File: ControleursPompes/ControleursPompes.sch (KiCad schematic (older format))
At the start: 54 parts, among them J1 SWD, J2 PWR_IN, J3 I2C 5V, J4 I2C 3.3V, J5 ARIG Interf, Q1 BSS138, Q2 BSS138, SW1 Reset, SW2 Reset, SW3 Reset, U1 AMS1117-3.3, U2 STM32F103C8Tx, Y1 16Mhz

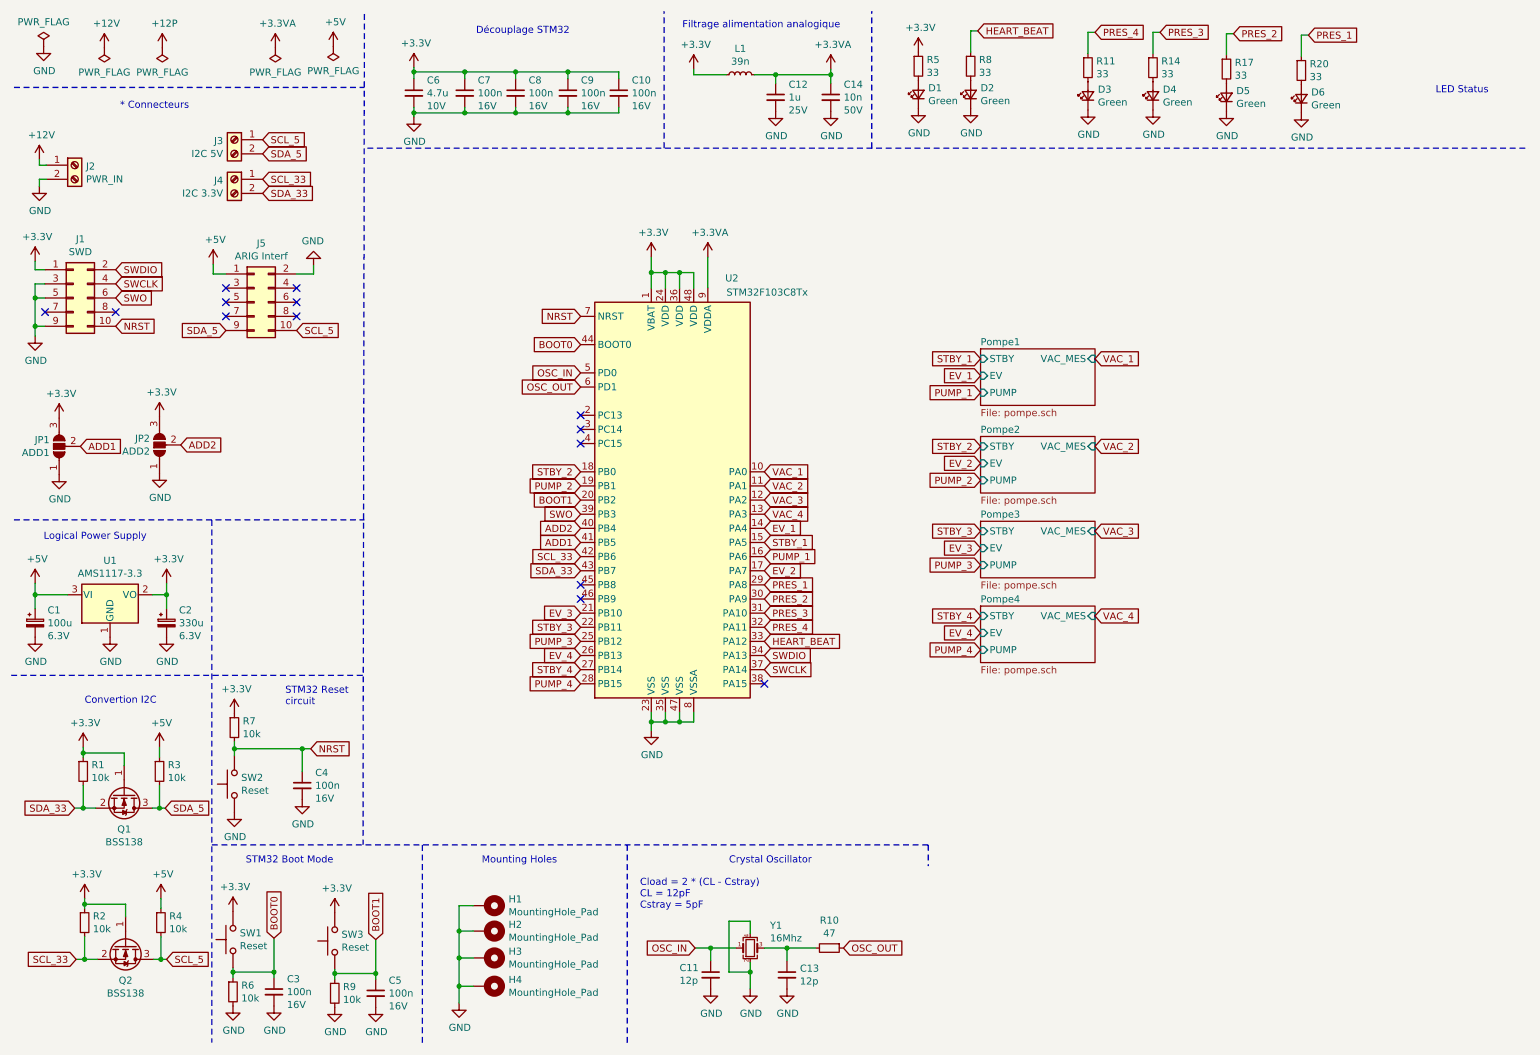
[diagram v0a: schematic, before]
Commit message: Ajout bornier alim 5V sur controleur pompes
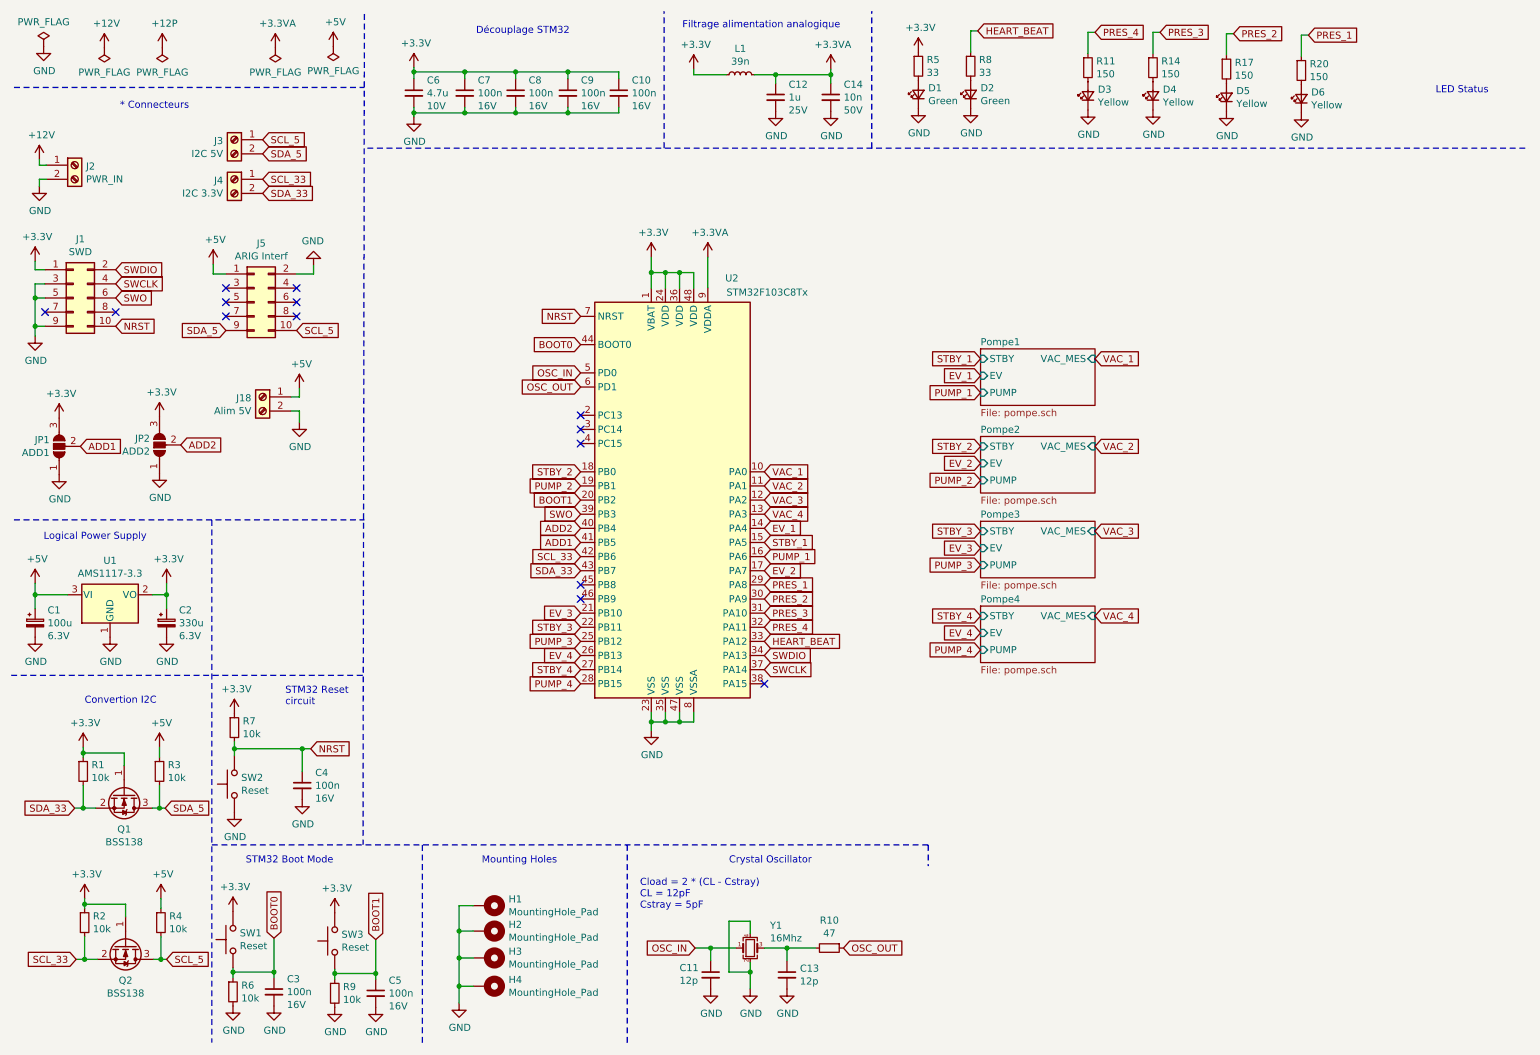
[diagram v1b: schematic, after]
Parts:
- added J18: Alim 5V, TerminalBlock_Phoenix:TerminalBlock_Phoenix_MPT-0,5-2-2.54_1x02_P2.54mm_Horizontal, symbol Connector:Screw_Terminal_01x02
- D3, D4, D5, D6: value Green -> Yellow; LCSC Part C63855 -> C74346
- R11, R14, R17, R20: value 33 -> 150; LCSC Part C17634 -> C17471
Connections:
- net +5V: now also J18.1 (Pin_1)
- net GND: now also J18.2 (Pin_2)
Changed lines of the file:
@@
 P 8100 880
 F 0 "R11" H 8159 926 50  0000 L CNN
-F 1 "33" H 8159 835 50  0000 L CNN
+F 1 "150" H 8159 835 50  0000 L CNN
 F 2 "Resistor_SMD:R_0805_2012Metric_Pad1.20x1.40mm_HandSolder" H 8100 880 50  0001 C CNN
 F 3 "~" H 8100 880 50  0001 C CNN
-F 4 "C17634" H 8100 880 50  0001 C CNN "LCSC Part"
+F 4 "C17471" H 8100 880 50  0001 C CNN "LCSC Part"
 	1    8100 880
 	1    0    0    -1
@@
 P 8100 1080
 F 0 "D3" V 8146 1010 50  0000 R CNN
-F 1 "Green" V 8055 1010 50  0000 R CNN
+F 1 "Yellow" V 8055 1010 50  0000 R CNN
 F 2 "LED_SMD:LED_0805_2012Metric_Pad1.15x1.40mm_HandSolder" V 8100 1080 50  0001 C CNN
 F 3 "~" V 8100 1080 50  0001 C CNN
-F 4 "C63855" H 8100 1080 50  0001 C CNN "LCSC Part"
+F 4 "C74346" H 8100 1080 50  0001 C CNN "LCSC Part"
 	1    8100 1080
 	0    -1   -1   0
@@
 P 8560 880
 F 0 "R14" H 8619 926 50  0000 L CNN
-F 1 "33" H 8619 835 50  0000 L CNN
+F 1 "150" H 8619 835 50  0000 L CNN
 F 2 "Resistor_SMD:R_0805_2012Metric_Pad1.20x1.40mm_HandSolder" H 8560 880 50  0001 C CNN
 F 3 "~" H 8560 880 50  0001 C CNN
-F 4 "C17634" H 8560 880 50  0001 C CNN "LCSC Part"
+F 4 "C17471" H 8560 880 50  0001 C CNN "LCSC Part"
 	1    8560 880
 	1    0    0    -1
@@
 P 8560 1080
 F 0 "D4" V 8606 1010 50  0000 R CNN
-F 1 "Green" V 8515 1010 50  0000 R CNN
+F 1 "Yellow" V 8515 1010 50  0000 R CNN
 F 2 "LED_SMD:LED_0805_2012Metric_Pad1.15x1.40mm_HandSolder" V 8560 1080 50  0001 C CNN
 F 3 "~" V 8560 1080 50  0001 C CNN
-F 4 "C63855" H 8560 1080 50  0001 C CNN "LCSC Part"
+F 4 "C74346" H 8560 1080 50  0001 C CNN "LCSC Part"
 	1    8560 1080
 	0    -1   -1   0
@@
 P 9080 890
 F 0 "R17" H 9139 936 50  0000 L CNN
-F 1 "33" H 9139 845 50  0000 L CNN
+F 1 "150" H 9139 845 50  0000 L CNN
 F 2 "Resistor_SMD:R_0805_2012Metric_Pad1.20x1.40mm_HandSolder" H 9080 890 50  0001 C CNN
 F 3 "~" H 9080 890 50  0001 C CNN
-F 4 "C17634" H 9080 890 50  0001 C CNN "LCSC Part"
+F 4 "C17471" H 9080 890 50  0001 C CNN "LCSC Part"
 	1    9080 890
 	1    0    0    -1
@@
 P 9080 1090
 F 0 "D5" V 9126 1020 50  0000 R CNN
-F 1 "Green" V 9035 1020 50  0000 R CNN
+F 1 "Yellow" V 9035 1020 50  0000 R CNN
 F 2 "LED_SMD:LED_0805_2012Metric_Pad1.15x1.40mm_HandSolder" V 9080 1090 50  0001 C CNN
 F 3 "~" V 9080 1090 50  0001 C CNN
-F 4 "C63855" H 9080 1090 50  0001 C CNN "LCSC Part"
+F 4 "C74346" H 9080 1090 50  0001 C CNN "LCSC Part"
 	1    9080 1090
 	0    -1   -1   0
@@
 P 9610 900
 F 0 "R20" H 9669 946 50  0000 L CNN
-F 1 "33" H 9669 855 50  0000 L CNN
+F 1 "150" H 9669 855 50  0000 L CNN
 F 2 "Resistor_SMD:R_0805_2012Metric_Pad1.20x1.40mm_HandSolder" H 9610 900 50  0001 C CNN
 F 3 "~" H 9610 900 50  0001 C CNN
-F 4 "C17634" H 9610 900 50  0001 C CNN "LCSC Part"
+F 4 "C17471" H 9610 900 50  0001 C CNN "LCSC Part"
 	1    9610 900
 	1    0    0    -1
@@
 P 9610 1100
 F 0 "D6" V 9656 1030 50  0000 R CNN
-F 1 "Green" V 9565 1030 50  0000 R CNN
+F 1 "Yellow" V 9565 1030 50  0000 R CNN
 F 2 "LED_SMD:LED_0805_2012Metric_Pad1.15x1.40mm_HandSolder" V 9610 1100 50  0001 C CNN
 F 3 "~" V 9610 1100 50  0001 C CNN
-F 4 "C63855" H 9610 1100 50  0001 C CNN "LCSC Part"
+F 4 "C74346" H 9610 1100 50  0001 C CNN "LCSC Part"
 	1    9610 1100
 	0    -1   -1   0
@@
 Wire Notes Line
 	3000 1450 11220 1450
+$Comp
+L Connector:Screw_Terminal_01x02 J18
+U 1 1 60671C10
+P 2260 3210
+F 0 "J18" H 2340 3202 50  0000 L CNN
+F 1 "Alim 5V" H 2340 3111 50  0000 L CNN
+F 2 "TerminalBlock_Phoenix:TerminalBlock_Phoenix_MPT-0,5-2-2.54_1x02_P2.54mm_Horizontal" H 2260 3210 50  0001 C CNN
+F 3 "~" H 2260 3210 50  0001 C CNN
+F 4 "0" H 2260 3210 50  0001 C CNN "JLCPCB BOM"
+	1    2260 3210
+	-1   0    0    -1
+$EndComp
+$Comp
+L power:+5V #PWR0112
+U 1 1 60672896
+P 2520 3150
+F 0 "#PWR0112" H 2520 3000 50  0001 C CNN
+F 1 "+5V" H 2535 3323 50  0000 C CNN
+F 2 "" H 2520 3150 50  0001 C CNN
+F 3 "" H 2520 3150 50  0001 C CNN
+	1    2520 3150
+	1    0    0    -1
+$EndComp
+$Comp
+L power:GND #PWR0113
+U 1 1 60673243
+P 2520 3390
+F 0 "#PWR0113" H 2520 3140 50  0001 C CNN
+F 1 "GND" H 2525 3217 50  0000 C CNN
+F 2 "" H 2520 3390 50  0001 C CNN
+F 3 "" H 2520 3390 50  0001 C CNN
+	1    2520 3390
+	1    0    0    -1
+$EndComp
+Wire Wire Line
+	2460 3210 2520 3210
+Wire Wire Line
+	2520 3210 2520 3150
+Wire Wire Line
+	2460 3310 2520 3310
+Wire Wire Line
+	2520 3310 2520 3390
 $EndSCHEMATC

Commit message: Ajout 4 inputs TOR sur le contrôleur pompes
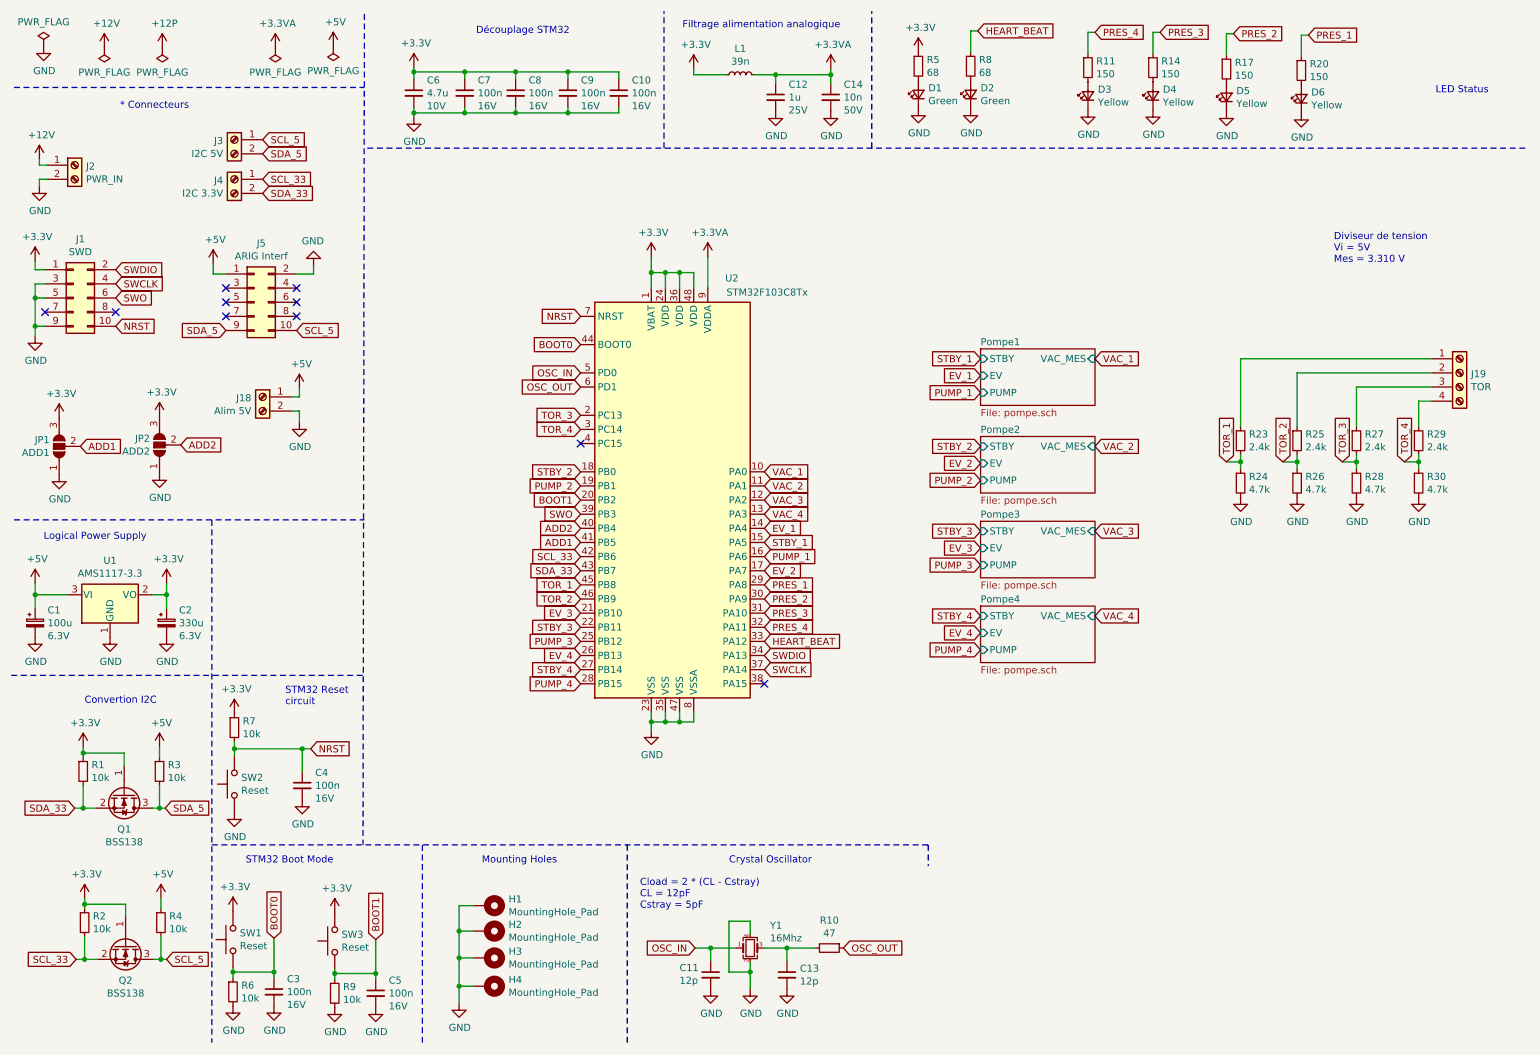
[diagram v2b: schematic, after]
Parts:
- added J19: TOR, TerminalBlock_Phoenix:TerminalBlock_Phoenix_MPT-0,5-4-2.54_1x04_P2.54mm_Horizontal, symbol Connector:Screw_Terminal_01x04
- added R23, R25, R27, R29: 2.4k, Resistor_SMD:R_0805_2012Metric_Pad1.20x1.40mm_HandSolder, symbol Device:R_Small
- added R24, R26, R28, R30: 4.7k, Resistor_SMD:R_0805_2012Metric_Pad1.20x1.40mm_HandSolder, symbol Device:R_Small
- Q1, Q2: LCSC Part C112239 -> C426569
- R5, R8: value 33 -> 68; LCSC Part C17634 -> C17802
- SW1, SW2, SW3: footprint Button_Switch_SMD:SW_SPST_B3U-1000P -> ARIG:SW_TS_1088_AR_3x4x2; LCSC Part C231329 -> C720477
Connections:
- net GND: now also R24.2, R26.2, R28.2, R30.2
- net TOR_3: now reaches U2.2 (PC13)
- net TOR_3: now also R27.2, R28.1
- net TOR_4: now reaches U2.3 (PC14)
- net TOR_4: now also R29.2, R30.1
- net TOR_1: now reaches U2.45 (PB8)
- net TOR_1: now also R23.2, R24.1
- net TOR_2: now reaches U2.46 (PB9)
- net TOR_2: now also R25.2, R26.1
- new net: J19.1 (Pin_1), R23.1
- new net: J19.2 (Pin_2), R25.1
- new net: J19.3 (Pin_3), R27.1
- new net: J19.4 (Pin_4), R29.1
- no-connect marks 14 -> 10
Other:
- note added: "Diviseur de tension\nVi = 5V\nMes = 3.310 V"
